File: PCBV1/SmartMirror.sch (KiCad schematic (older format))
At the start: 0 parts

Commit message: Finished video signals, added HDMI and SD connectors.
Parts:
- added C?: 100n, Capacitor_SMD:C_0603_1608Metric, symbol Device:C
- added C?: 22u, Capacitor_SMD:C_0603_1608Metric, symbol Device:C
- added J?: HDMI_A, symbol Connector:HDMI_A
- added J?: Amphenol GSD09002SEU, Personal_Misc:GSD09002SEU, symbol Connector:SD_Card
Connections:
- net labels added: +3V3, +5V, GND
- wire segments 49 -> 121
- no-connect marks 0 -> 5
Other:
- note added: "5V POWER FROM USB"
- note added: "PULL-UPS OR ESD PROTECTION"
- note removed: "HDMI connector"

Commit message: Added SD filter and USB-to-UART IC.
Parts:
- added J?: USB_B_Mini, symbol Connector:USB_B_Mini
- added U?: CM1624-08DE, Personal_Passives:CM1624, symbol Personal_Passives:CM1624-08DE
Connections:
- wire segments 121 -> 133
- no-connect marks 5 -> 9
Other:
- note added: "ADD LED FOR POWER"
- note added: "ESD diodes for D+, D-, VBUS\nLED for VBUS\n"
- note removed: "5V POWER FROM USB"
- note removed: "PULL-UPS OR ESD PROTECTION"
- note removed: "USB connector"
- moved on the sheet: C?, J?

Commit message: Changed note.
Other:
- note added: "ADD 5V SUPPLY (NOT USB)"
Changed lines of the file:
@@
 Wire Wire Line
 	5800 3250 5300 3250
-$Comp
-L power:+5V #PWR?
-U 1 1 62777497
-P 4900 4300
-F 0 "#PWR?" H 4900 4150 50  0001 C CNN
-F 1 "+5V" H 4915 4473 50  0000 C CNN
-F 2 "" H 4900 4300 50  0001 C CNN
-F 3 "" H 4900 4300 50  0001 C CNN
-	1    4900 4300
-	-1   0    0    1
-$EndComp
 Wire Wire Line
 	4900 4300 4900 4250
@@
 Text Notes 8750 1200 0    50   ~ 0
 ADD LED FOR POWER
+Text Notes 4450 4500 0    50   ~ 0
+ADD 5V SUPPLY (NOT USB)
 $EndSCHEMATC

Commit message: Many minor changes to component footprints and schematics.
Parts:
- removed J?: Amphenol GSD09002SEU, Personal_Misc:GSD09002SEU, symbol Connector:SD_Card
- removed J?: USB_B_Mini, symbol Connector:USB_B_Mini
- added C86: 100n, Capacitor_SMD:C_0603_1608Metric, symbol Device:C
- added D1: 150060SS55040, Personal_Passives:150060SS55040, symbol Personal_Passives:150060SS55040
- added J2: 502570-0893, Personal_Misc:502570-0893, symbol Personal_Misc:502570-0893
- added J3: 10118194-0001LF, Personal_Misc:10118194-0001LF, symbol Personal_Misc:10118194-0001LF
- added R1: 520, Resistor_SMD:R_0603_1608Metric, symbol Device:R
- added U2: TPD3E001DRLR, Package_TO_SOT_SMD:SOT-553, symbol Power_Protection:TPD3E001DRLR
- J1: renamed from J?; value HDMI_A -> 208658-1051; footprint (none) -> Personal_Misc:2086581051
- gave numbers to parts that had none: 3
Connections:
- net labels added: +5V_USB
- wire segments 133 -> 163
- no-connect marks 9 -> 10
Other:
- note removed: "ADD 5V SUPPLY (NOT USB)"
- note removed: "ADD LED FOR POWER"
- note removed: "ESD diodes for D+, D-, VBUS\nLED for VBUS\n"
- moved on the sheet: C1, C2

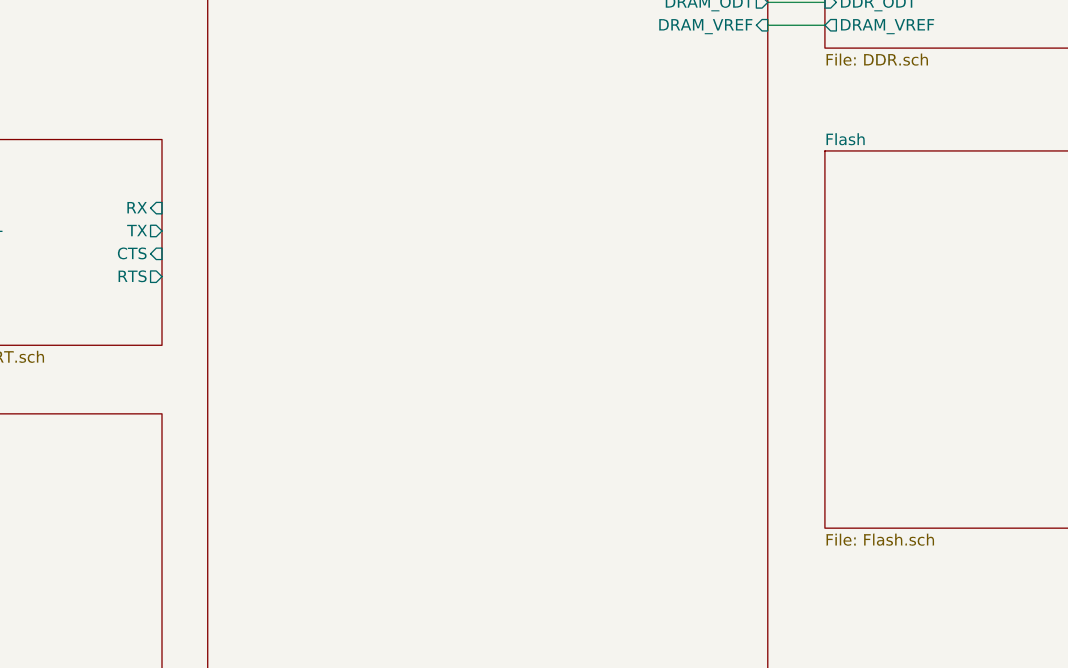
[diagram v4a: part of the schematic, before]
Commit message: Added NAND flash with connections, updated IO config.
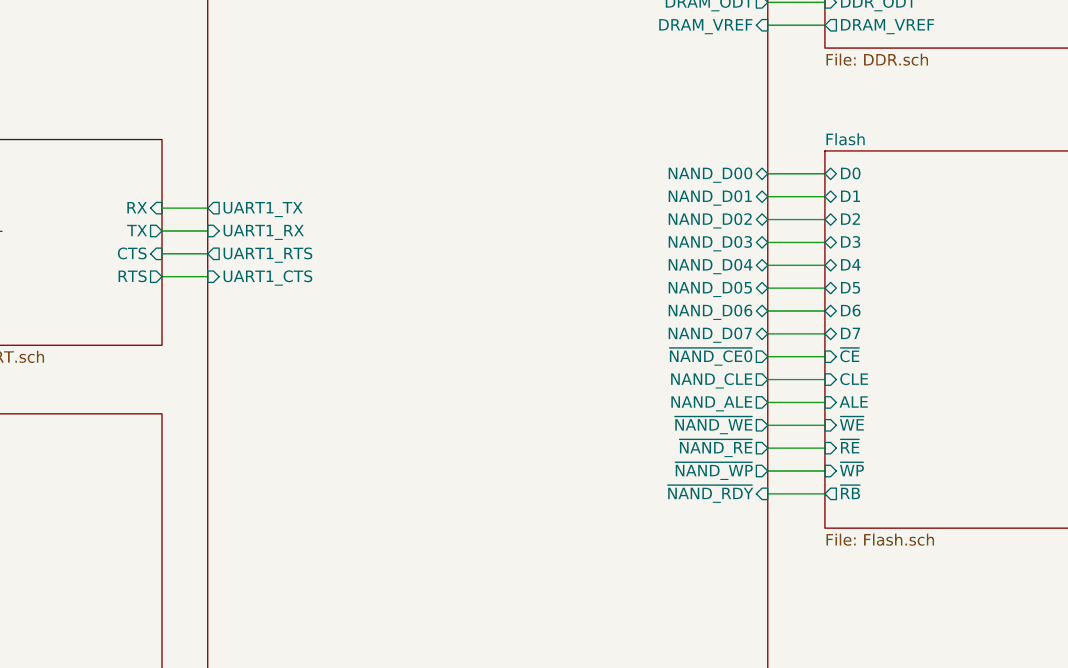
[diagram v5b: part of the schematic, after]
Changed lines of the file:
@@
 F0 "Flash" 50
 F1 "Flash.sch" 50
+F2 "~WP" I L 9700 8650 50
+F3 "ALE" I L 9700 8350 50
+F4 "~CE" I L 9700 8150 50
+F5 "~WE" I L 9700 8450 50
+F6 "~RB" O L 9700 8750 50
+F7 "~RE" I L 9700 8550 50
+F8 "CLE" I L 9700 8250 50
+F9 "D0" B L 9700 7350 50
+F10 "D1" B L 9700 7450 50
+F11 "D5" B L 9700 7850 50
+F12 "D7" B L 9700 8050 50
+F13 "D2" B L 9700 7550 50
+F14 "D3" B L 9700 7650 50
+F15 "D4" B L 9700 7750 50
+F16 "D6" B L 9700 7950 50
 $EndSheet
 $Sheet
@@
 F85 "LCD_D10" O L 7000 3000 50
 F86 "LCD_RESET" O L 7000 4500 50
+F87 "UART1_RTS" O L 7000 7700 50
+F88 "UART1_TX" O L 7000 7500 50
+F89 "UART1_RX" I L 7000 7600 50
+F90 "UART1_CTS" I L 7000 7800 50
+F91 "NAND_D07" B R 9450 8050 50
+F92 "NAND_D06" B R 9450 7950 50
+F93 "NAND_D02" B R 9450 7550 50
+F94 "NAND_CLE" O R 9450 8250 50
+F95 "~NAND_RDY" I R 9450 8750 50
+F96 "NAND_ALE" O R 9450 8350 50
+F97 "NAND_D05" B R 9450 7850 50
+F98 "NAND_D01" B R 9450 7450 50
+F99 "~NAND_CE0" O R 9450 8150 50
+F100 "NAND_D04" B R 9450 7750 50
+F101 "~NAND_WE" O R 9450 8450 50
+F102 "~NAND_WP" O R 9450 8650 50
+F103 "NAND_D03" B R 9450 7650 50
+F104 "NAND_D00" B R 9450 7350 50
+F105 "~NAND_RE" O R 9450 8550 50
 $EndSheet
 Wire Wire Line
@@
 $EndComp
 Connection ~ 4700 6750
+Wire Wire Line
+	6800 7800 7000 7800
+Wire Wire Line
+	7000 7700 6800 7700
+Wire Wire Line
+	6800 7600 7000 7600
+Wire Wire Line
+	7000 7500 6800 7500
+Wire Wire Line
+	9450 7350 9700 7350
+Wire Wire Line
+	9700 7450 9450 7450
+Wire Wire Line
+	9450 7550 9700 7550
+Wire Wire Line
+	9700 7650 9450 7650
+Wire Wire Line
+	9450 7750 9700 7750
+Wire Wire Line
+	9700 7850 9450 7850
+Wire Wire Line
+	9450 7950 9700 7950
+Wire Wire Line
+	9700 8050 9450 8050
+Wire Wire Line
+	9450 8150 9700 8150
+Wire Wire Line
+	9700 8250 9450 8250
+Wire Wire Line
+	9450 8350 9700 8350
+Wire Wire Line
+	9700 8450 9450 8450
+Wire Wire Line
+	9450 8550 9700 8550
+Wire Wire Line
+	9700 8650 9450 8650
+Wire Wire Line
+	9450 8750 9700 8750
 $EndSCHEMATC

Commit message: Laid final hands on Wi-Fi and all circuits. Started work on PCB.
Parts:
- added SW1: SW_DIP_x05, Button_Switch_SMD:SW_DIP_SPSTx05_Slide_6.7x14.26mm_W6.73mm_P2.54mm_LowProfile_JPin, symbol Switch:SW_DIP_x05
- renumbered C86 to C3, U1 to U3, U2 to U4
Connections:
- net Processor/~SD_CD is gone; now on an unnamed net: J2.DS1 (CD)
- net +3V3: now also SW1.1, SW1.2, SW1.3, SW1.4, SW1.5
- net Processor/LCD_D03: now also SW1.10
- net Processor/LCD_D04: now also SW1.9
- net Processor/LCD_D05: now also SW1.8
- net Processor/LCD_D06: now also SW1.7
- net Processor/LCD_D07: now also SW1.6
- net Processor/~SD1_CD: now reaches U3.13 (ESD1_2)
- net Processor/SD_CLK renamed Processor/SD1_CLK
- net Processor/SD_CMD renamed Processor/SD1_CMD
- net Processor/SD_D0 renamed Processor/SD1_D0
- net Processor/SD_D1 renamed Processor/SD1_D1
- net Processor/SD_D2 renamed Processor/SD1_D2
- net Processor/SD_D3 renamed Processor/SD1_D3
- no-connect marks 10 -> 8
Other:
- note added: "D[3:7] = BOOT_CFG[3:7]\nBootmodes:\n01000 = QSPI\n00000 = NOR\n00001 = OneNAND\n0011x = Serial-ROM\n01000 = SD (regular boot)\n01100 = MMC (regular boot)\n10000 = NAND"
- note added: "Tilføj Ethernet til RJ-45?"
- moved on the sheet: J1

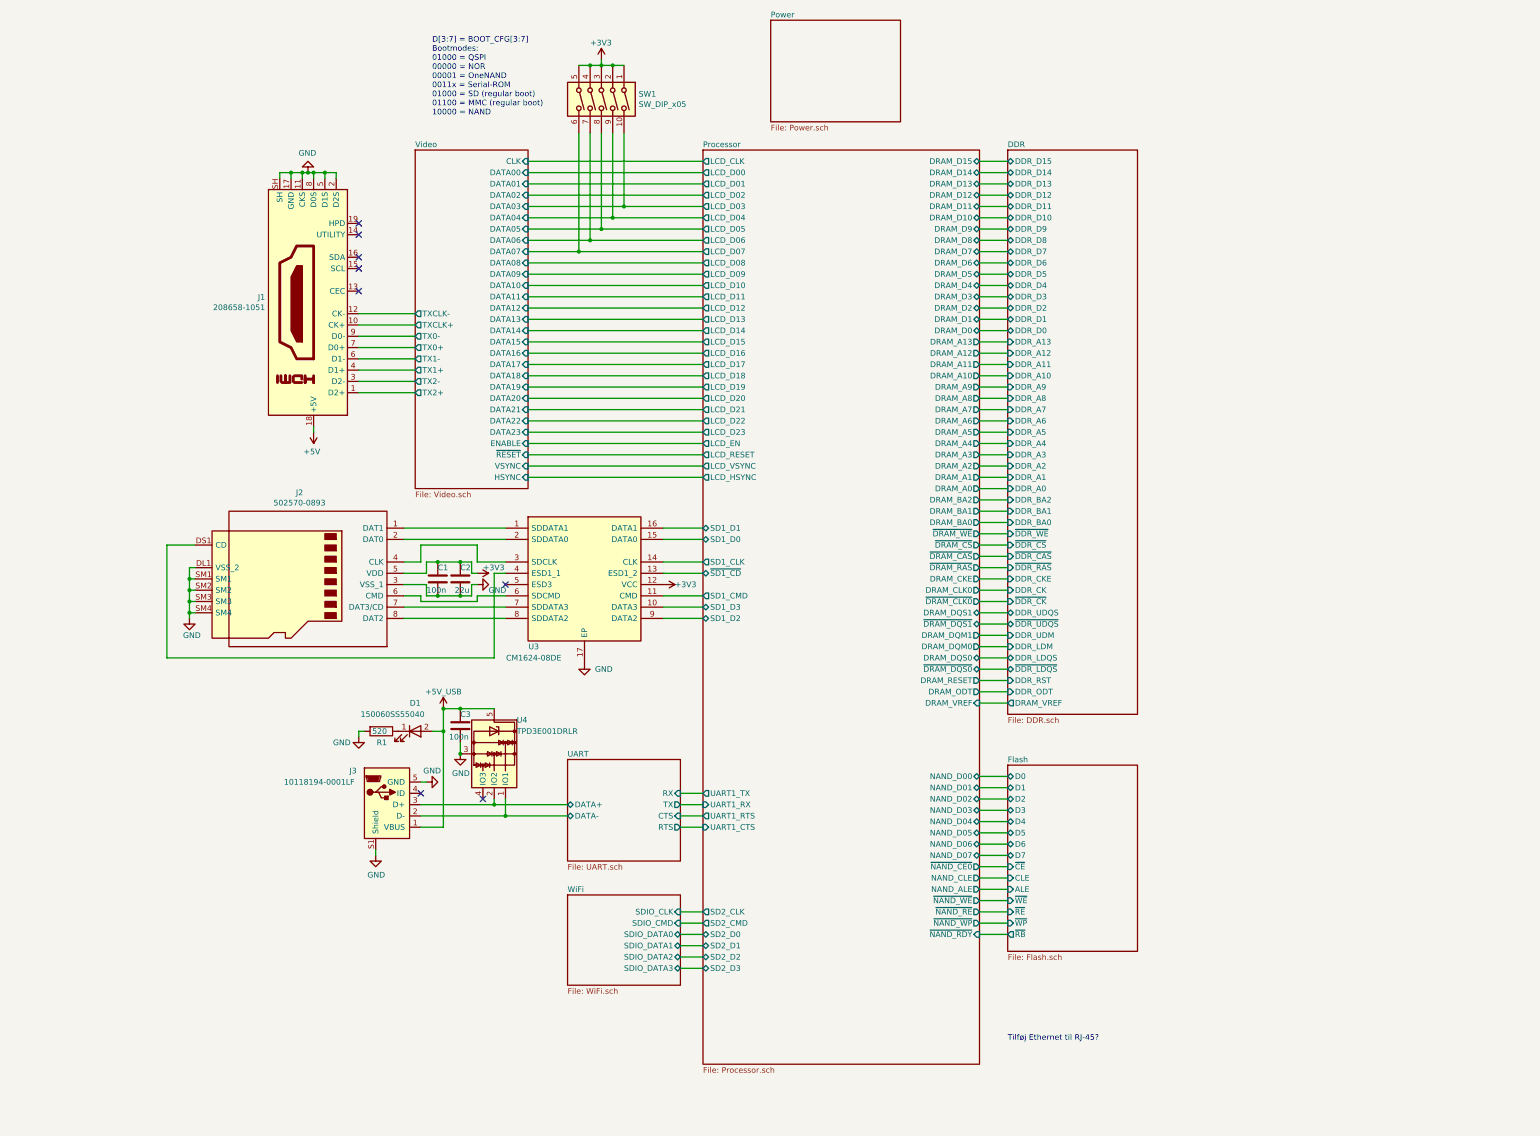
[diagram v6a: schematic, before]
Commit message: Added JTAG, USB OTG, USB Host, and Ethernet.
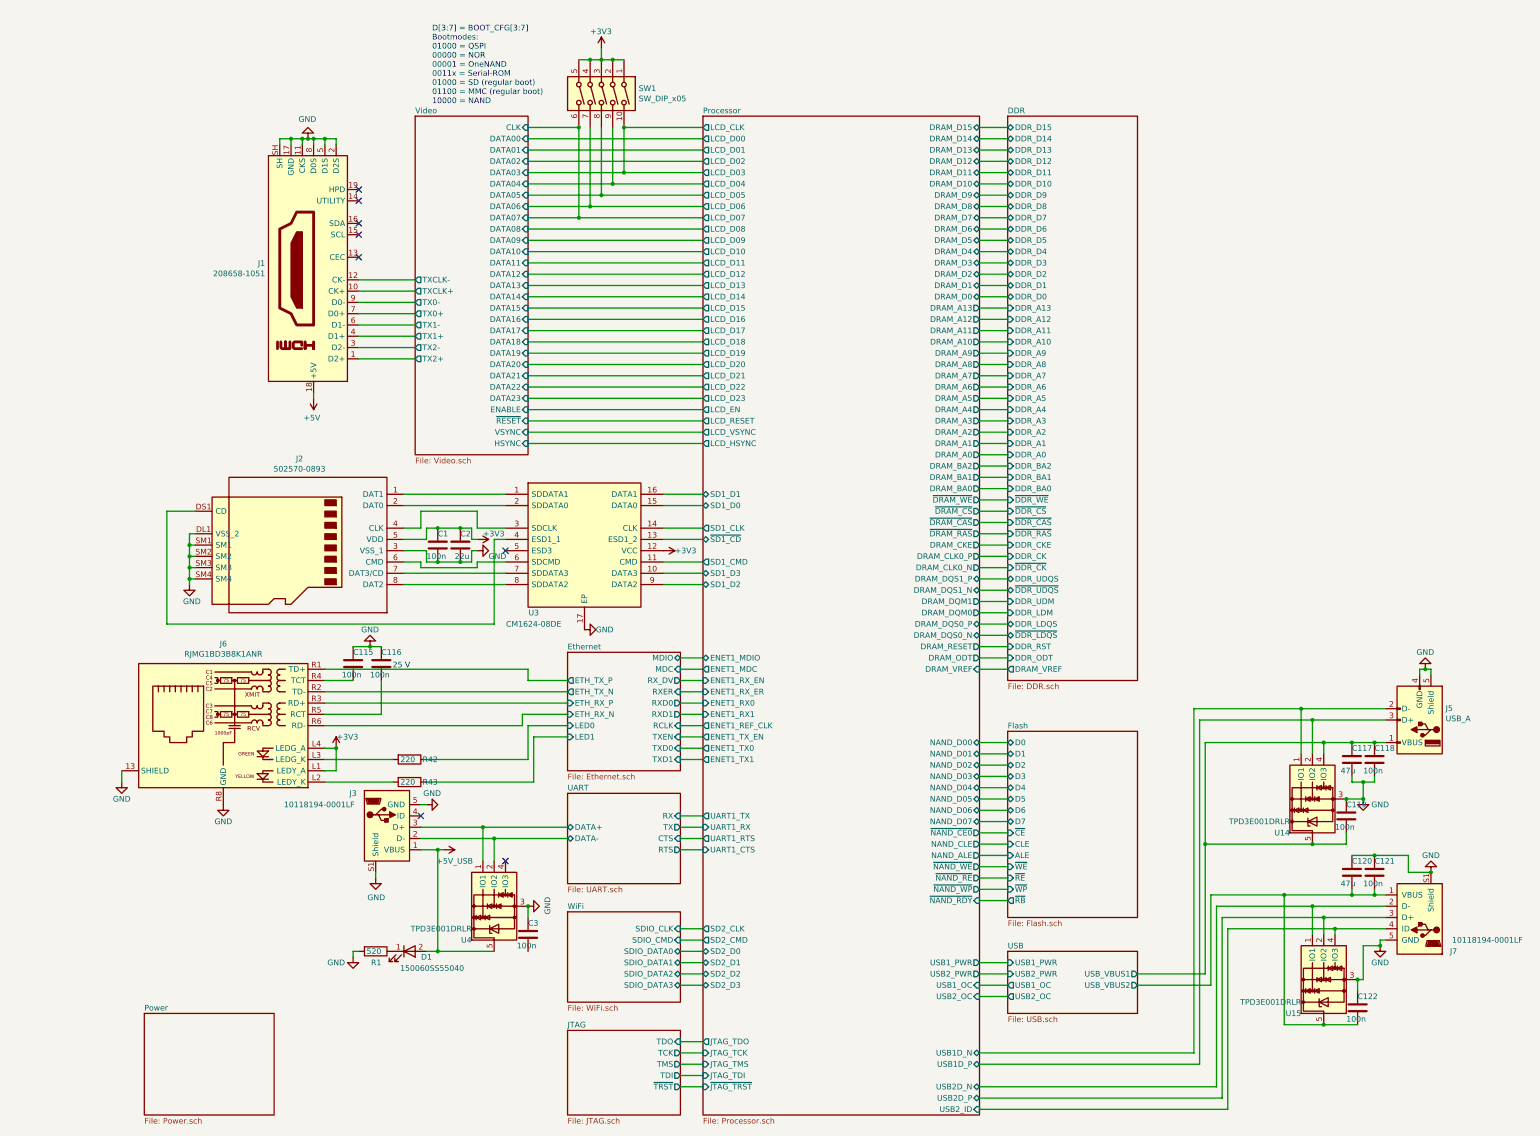
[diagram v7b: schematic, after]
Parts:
- added C115, C116, C118, C119, C121, C122: 100n, Capacitor_SMD:C_0603_1608Metric, symbol Device:C
- added C117, C120: 47u, Capacitor_SMD:C_0805_2012Metric, symbol Device:C
- added J5: USB_A, Connector_USB:USB_A_Molex_67643_Horizontal, symbol Connector:USB_A
- added J6: RJMG1BD3B8K1ANR, Personal_Misc:RJMG1BD3B8K1ANR, symbol Personal_Misc:RJMG1BD3B8K1ANR
- added J7: 10118194-0001LF, Personal_Misc:10118194-0001LF, symbol Personal_Misc:10118194-0001LF
- added R42, R43: 220, Resistor_SMD:R_0603_1608Metric, symbol Device:R
- added U14, U15: TPD3E001DRLR, Package_TO_SOT_SMD:SOT-553, symbol Power_Protection:TPD3E001DRLR
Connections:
- net Processor/LCD_D03 is gone; now on net Processor/LCD_CLK: SW1.10
- net +3V3: now also J6.L1 (LEDY_A), J6.L4 (LEDG_A)
- net +5V_USB: no longer C3.1
- net GND: now also C3.1, C115.1, C116.1, C117.2, C118.2, C119.1, C120.1, C121.1, C122.1, J5.4 (GND), J5.5 (Shield), J6.13 (SHIELD), J6.R8 (GND), J7.5 (GND), J7.S1 (Shield), U14.3, U15.3; no longer C3.2
- net UART/DATA+: now also U4.1 (IO1); no longer U4.2 (IO2)
- net UART/DATA-: now also U4.2 (IO2); no longer U4.1 (IO1)
- new net: J6.L3 (LEDG_K), R42.2
- new net: J6.L2 (LEDY_K), R43.2
- new net: C115.2, J6.R4 (TCT)
- new net: C116.2, J6.R5 (RCT)
- new net Ethernet/ETH_RX_N: J6.R6 (RD-)
- new net Ethernet/ETH_RX_P: J6.R3 (RD+)
- new net Ethernet/ETH_TX_N: J6.R2 (TD-)
- new net Ethernet/ETH_TX_P: J6.R1 (TD+)
- new net Ethernet/LED0: R42.1
- new net Ethernet/LED1: R43.1
- new net Processor/USB1D_N: J5.2 (D-), U14.1 (IO1)
- new net Processor/USB1D_P: J5.3 (D+), U14.2 (IO2)
- new net Processor/USB2D_N: J7.2 (D-), U15.1 (IO1)
- new net Processor/USB2D_P: J7.3 (D+), U15.2 (IO2)
- new net Processor/USB2_ID: J7.4 (ID), U15.4 (IO3)
- new net USB/USB_VBUS1: C117.1, C118.1, C119.2, J5.1 (VBUS), U14.4 (IO3), U14.5
- new net USB/USB_VBUS2: C120.2, C121.2, C122.2, J7.1 (VBUS), U15.5
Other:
- note added: "25 V"
- note removed: "Tilføj Ethernet til RJ-45?"
- moved on the sheet: C1, C2, C3, D1, J1, J2, J3, R1, SW1, U3, U4
